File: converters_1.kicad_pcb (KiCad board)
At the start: 4 copper layers, 95 x 100 mm, 179 parts, among them J1 +15V, J10 Conn_01x10, J11 Conn_01x10, J12 Conn_01x10, J13 Conn_01x02, J14 Conn_01x02, J15 Conn_01x02, J16 Conn_01x02, J17 REF, J18 AGND, J19 AGND, J2 GND, J20 DAC_OUT, J21 ADC2, J22 AGND, J23 ADC1, J24 AGND, J3 -15V, J4 Conn_01x03, J5 Conn_01x03, J6 Conn_01x03, J7 Conn_01x02, J8 Conn_01x02, J9 Conn_01x10, U1 LM317EMPX/NOPB, U10 DAC91001, U11 50k 0.1%, U12 ADA4522-2, U13 ADA4522-2, U14 ADA4522-2, U15 50k 0.1%, U16 50k 0.1%, U17 ADS131A02, U2 LM337_SOT223, U3 LM317EMPX/NOPB, U4 LM337_SOT223, U5 REF5050, U6 LM317EMPX/NOPB, U7 OPA333AID, U8 ADA4522-2, U9 ADA4522-2, Y1 ABLS-16.384MHZ-L4Q-T

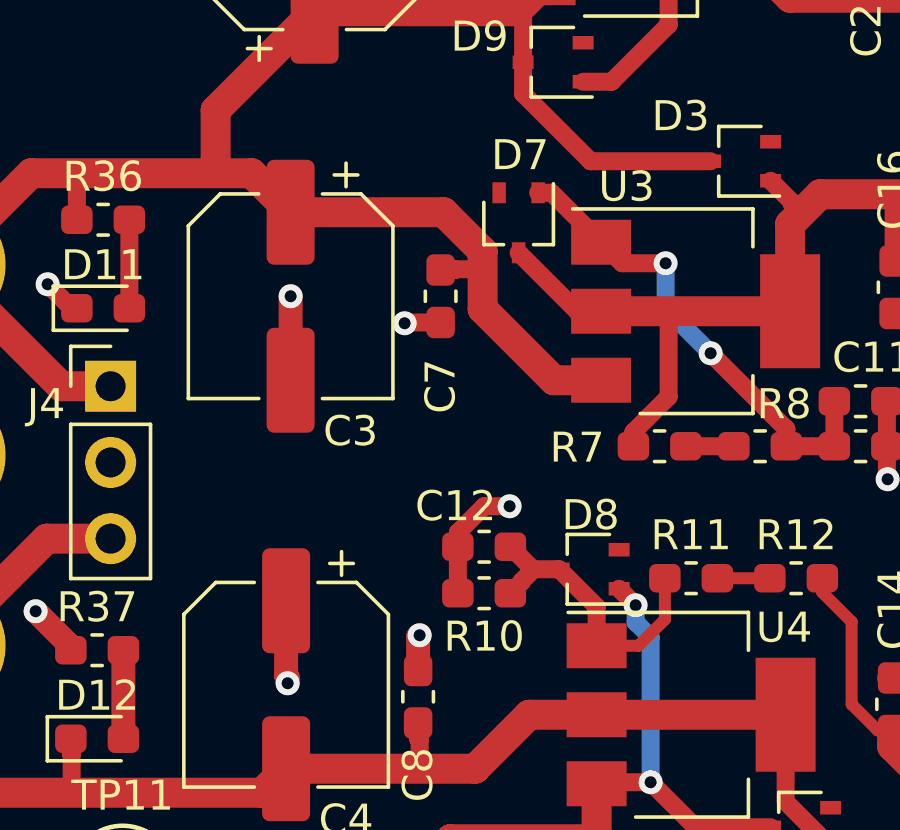
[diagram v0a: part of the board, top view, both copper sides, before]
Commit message: GND - AGND tie added
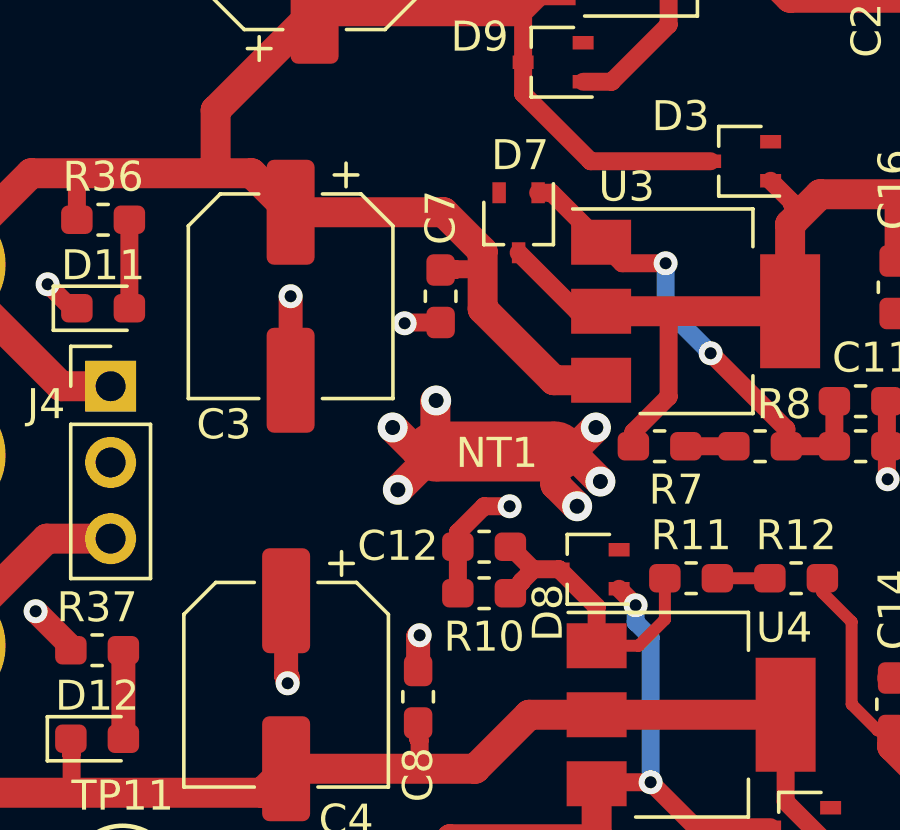
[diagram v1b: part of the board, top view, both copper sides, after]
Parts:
- added NT1: GND TIE, NetTie:NetTie-2_SMD_Pad2.0mm, F.Cu at (69.3, 50.7)
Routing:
- net GNDA: track 80.6 -> 86.4 mm, vias 34 -> 37
- net GND: track 173.7 -> 178.9 mm, vias 23 -> 26
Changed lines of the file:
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@@
     (thickness 1.6)
     (drawings 54)
-    (tracks 1396)
+    (tracks 1414)
     (zones 0)
-    (modules 179)
+    (modules 180)
     (nets 121)
   )
@@
   )
   (setup
-    (last_trace_width 0.4)
+    (last_trace_width 1)
     (user_trace_width 0.25)
     (user_trace_width 0.3)
@@
     (add_net "Net-(U7-Pad8)")
   )
+  (module NetTie:NetTie-2_SMD_Pad2.0mm (layer F.Cu)
+    (at 69.325 50.675)
+    (descr "Net tie, 2 pin, 2.0mm square SMD pads")
+    (tags "net tie")
+    (attr virtual)
+    (fp_text reference NT1 (at 0.05 0.05) (layer F.SilkS)
+      (effects (font (size 1 1) (thickness 0.15)))
+    )
+    (fp_text value "GND TIE" (at 0 2) (layer F.Fab)
+      (effects (font (size 1 1) (thickness 0.15)))
+    )
+    (fp_line (start -3.25 -1.25) (end 3.25 -1.25) (layer F.CrtYd) (width 0.05))
+    (fp_line (start 3.25 -1.25) (end 3.25 1.25) (layer F.CrtYd) (width 0.05))
+    (fp_line (start 3.25 1.25) (end -3.25 1.25) (layer F.CrtYd) (width 0.05))
+    (fp_line (start -3.25 1.25) (end -3.25 -1.25) (layer F.CrtYd) (width 0.05))
+    (fp_poly (pts (xy -2 -1) (xy 2 -1) (xy 2 1) (xy -2 1)) (layer F.Cu) (width 0))
+    (pad 2 smd circle (at 2 0) (size 2 2) (layers F.Cu)
+      (net 1 GNDA))
+    (pad 1 smd circle (at -2 0) (size 2 2) (layers F.Cu)
+      (net 4 GND))
+  )
   (module Package_DFN_QFN:DFN-8-1EP_4x4mm_P0.8mm_EP2.3x3.24mm (layer F.Cu)
     (at 100.1 93.9 180)
@@
     (tags "resistor handsolder")
     (attr smd)
-    (fp_text reference R7 (at -2.75 0.05) (layer F.SilkS)
+    (fp_text reference R7 (at 0.55 1.45) (layer F.SilkS)
       (effects (font (size 1 1) (thickness 0.15)))
     )
@@
     (tags "SOT-323 SC-70")
     (attr smd)
-    (fp_text reference D8 (at -0.05 1.8) (layer F.SilkS)
+    (fp_text reference D8 (at 1.375 -1.45 90) (layer F.SilkS)
       (effects (font (size 1 1) (thickness 0.15)))
     )
@@
     (tags "capacitor handsolder")
     (attr smd)
-    (fp_text reference C12 (at 0.95 1.35) (layer F.SilkS)
+    (fp_text reference C12 (at 2.875 0.025) (layer F.SilkS)
       (effects (font (size 1 1) (thickness 0.15)))
     )
@@
     (tags "capacitor handsolder")
     (attr smd)
-    (fp_text reference C7 (at -3 0 90) (layer F.SilkS)
+    (fp_text reference C7 (at 2.625 0 90) (layer F.SilkS)
       (effects (font (size 1 1) (thickness 0.15)))
     )
@@
     (tags "capacitor electrolytic")
     (attr smd)
-    (fp_text reference C3 (at 4.5 -2 180) (layer F.SilkS)
+    (fp_text reference C3 (at 4.275 2.225 180) (layer F.SilkS)
       (effects (font (size 1 1) (thickness 0.15)))
     )
@@
   (segment (start 103.65 64.475) (end 104.75 64.475) (width 0.6) (layer F.Cu) (net 1))
   (segment (start 104.75 64.475) (end 104.925 64.65) (width 0.6) (layer F.Cu) (net 1))
+  (via (at 72.825 51.675) (size 1) (drill 0.5) (layers F.Cu B.Cu) (net 1))
+  (segment (start 71.325 50.675) (end 71.825 50.675) (width 1) (layer F.Cu) (net 1))
+  (segment (start 71.825 50.675) (end 72.825 51.675) (width 1) (layer F.Cu) (net 1))
+  (via (at 72.05 52.5) (size 1) (drill 0.5) (layers F.Cu B.Cu) (net 1))
+  (segment (start 71.325 50.675) (end 71.325 51.775) (width 1) (layer F.Cu) (net 1))
+  (segment (start 71.325 51.775) (end 72.05 52.5) (width 1) (layer F.Cu) (net 1))
+  (via (at 72.675 49.875) (size 1) (drill 0.5) (layers F.Cu B.Cu) (net 1))
+  (segment (start 71.325 50.675) (end 71.875 50.675) (width 1) (layer F.Cu) (net 1))
+  (segment (start 71.875 50.675) (end 72.675 49.875) (width 1) (layer F.Cu) (net 1))
   (segment (start 72.85 46) (end 79.15 46) (width 1) (layer F.Cu) (net 2))
   (segment (start 79.15 43.1) (end 80.15 42.1) (width 1) (layer F.Cu) (net 2))
@@
   (segment (start 96.40763 84.5) (end 99.757641 81.149989) (width 0.25) (layer In2.GND) (net 4))
   (segment (start 98.225 80.7) (end 100.10765 80.7) (width 0.25) (layer F.Cu) (net 4))
+  (via (at 67.35 48.975) (size 1) (drill 0.5) (layers F.Cu B.Cu) (net 4))
+  (segment (start 67.325 50.675) (end 67.325 49) (width 1) (layer F.Cu) (net 4))
+  (segment (start 67.325 49) (end 67.35 48.975) (width 1) (layer F.Cu) (net 4))
+  (via (at 66.075 51.95) (size 1) (drill 0.5) (layers F.Cu B.Cu) (net 4))
+  (segment (start 67.325 50.675) (end 67.325 50.7) (width 1) (layer F.Cu) (net 4))
+  (segment (start 67.325 50.7) (end 66.075 51.95) (width 1) (layer F.Cu) (net 4))
+  (via (at 65.9 49.875) (size 1) (drill 0.5) (layers F.Cu B.Cu) (net 4))
+  (segment (start 67.325 50.675) (end 66.7 50.675) (width 1) (layer F.Cu) (net 4))
+  (segment (start 66.7 50.675) (end 65.9 49.875) (width 1) (layer F.Cu) (net 4))
   (segment (start 50.8 44.45) (end 53.85 41.4) (width 1) (layer F.Cu) (net 5))
   (segment (start 61.2 41.4) (end 62.5 42.7) (width 1) (layer F.Cu) (net 5))
